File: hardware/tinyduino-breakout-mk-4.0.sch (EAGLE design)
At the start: 3 parts

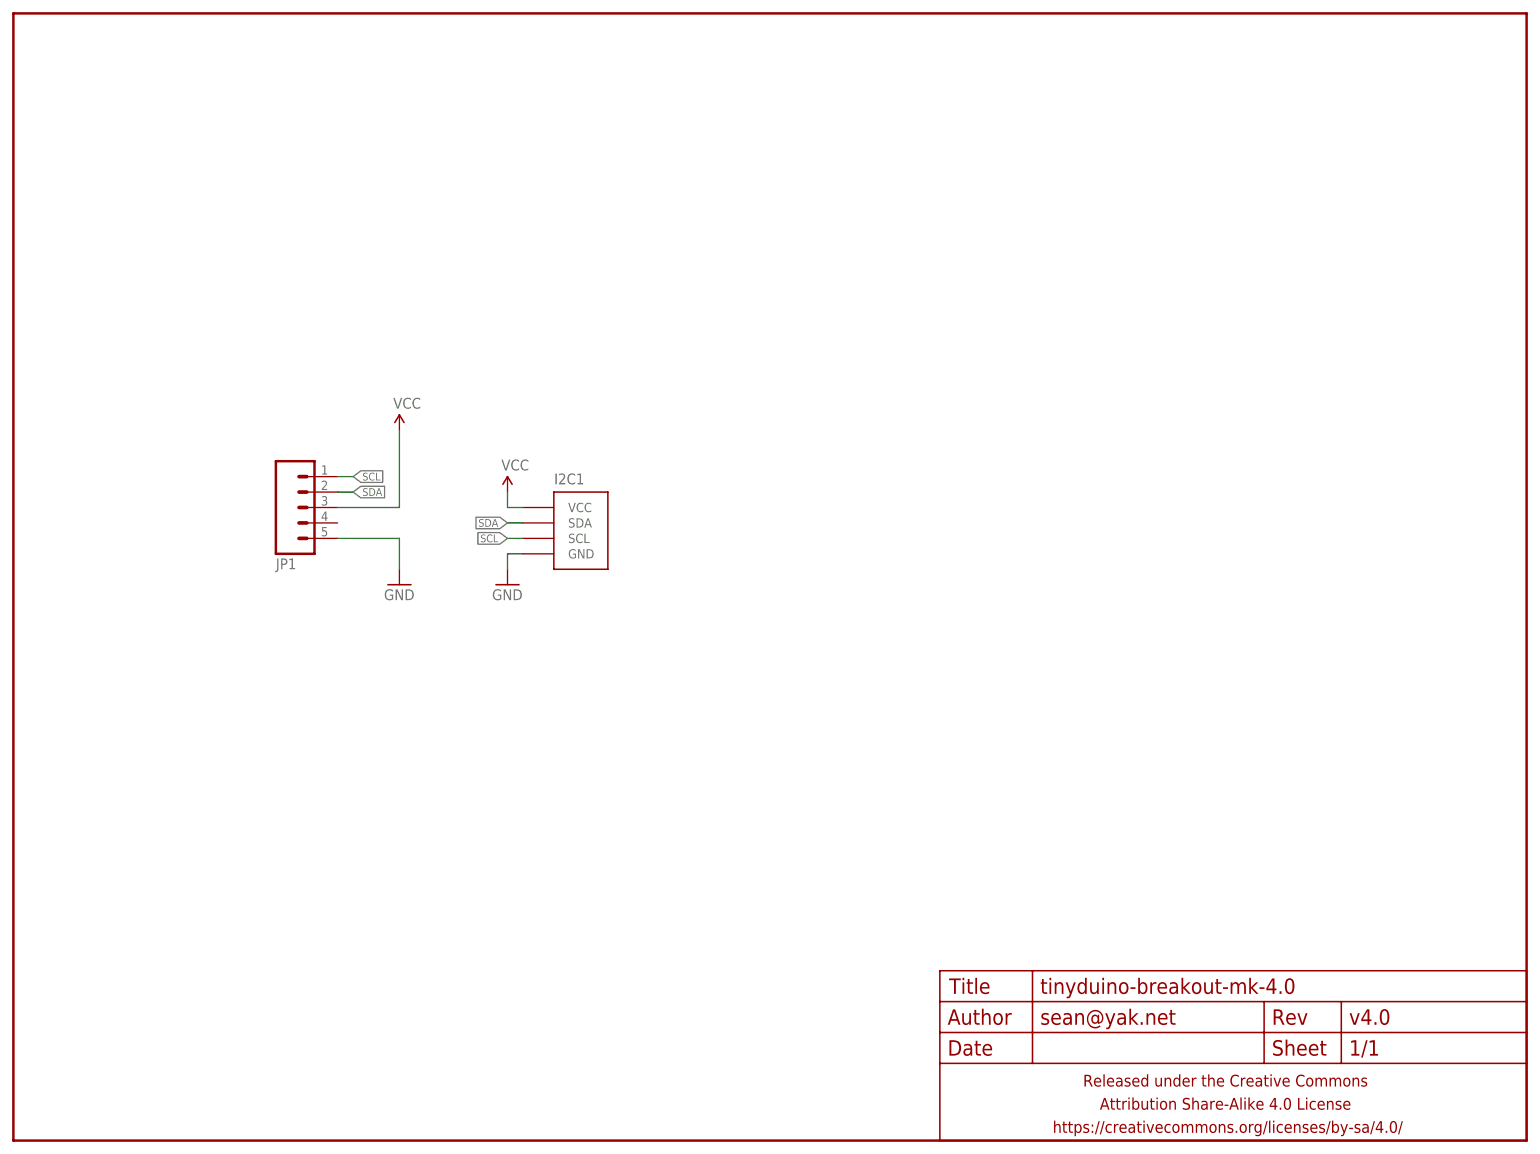
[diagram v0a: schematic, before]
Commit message: finished layout but unhappy w/choices
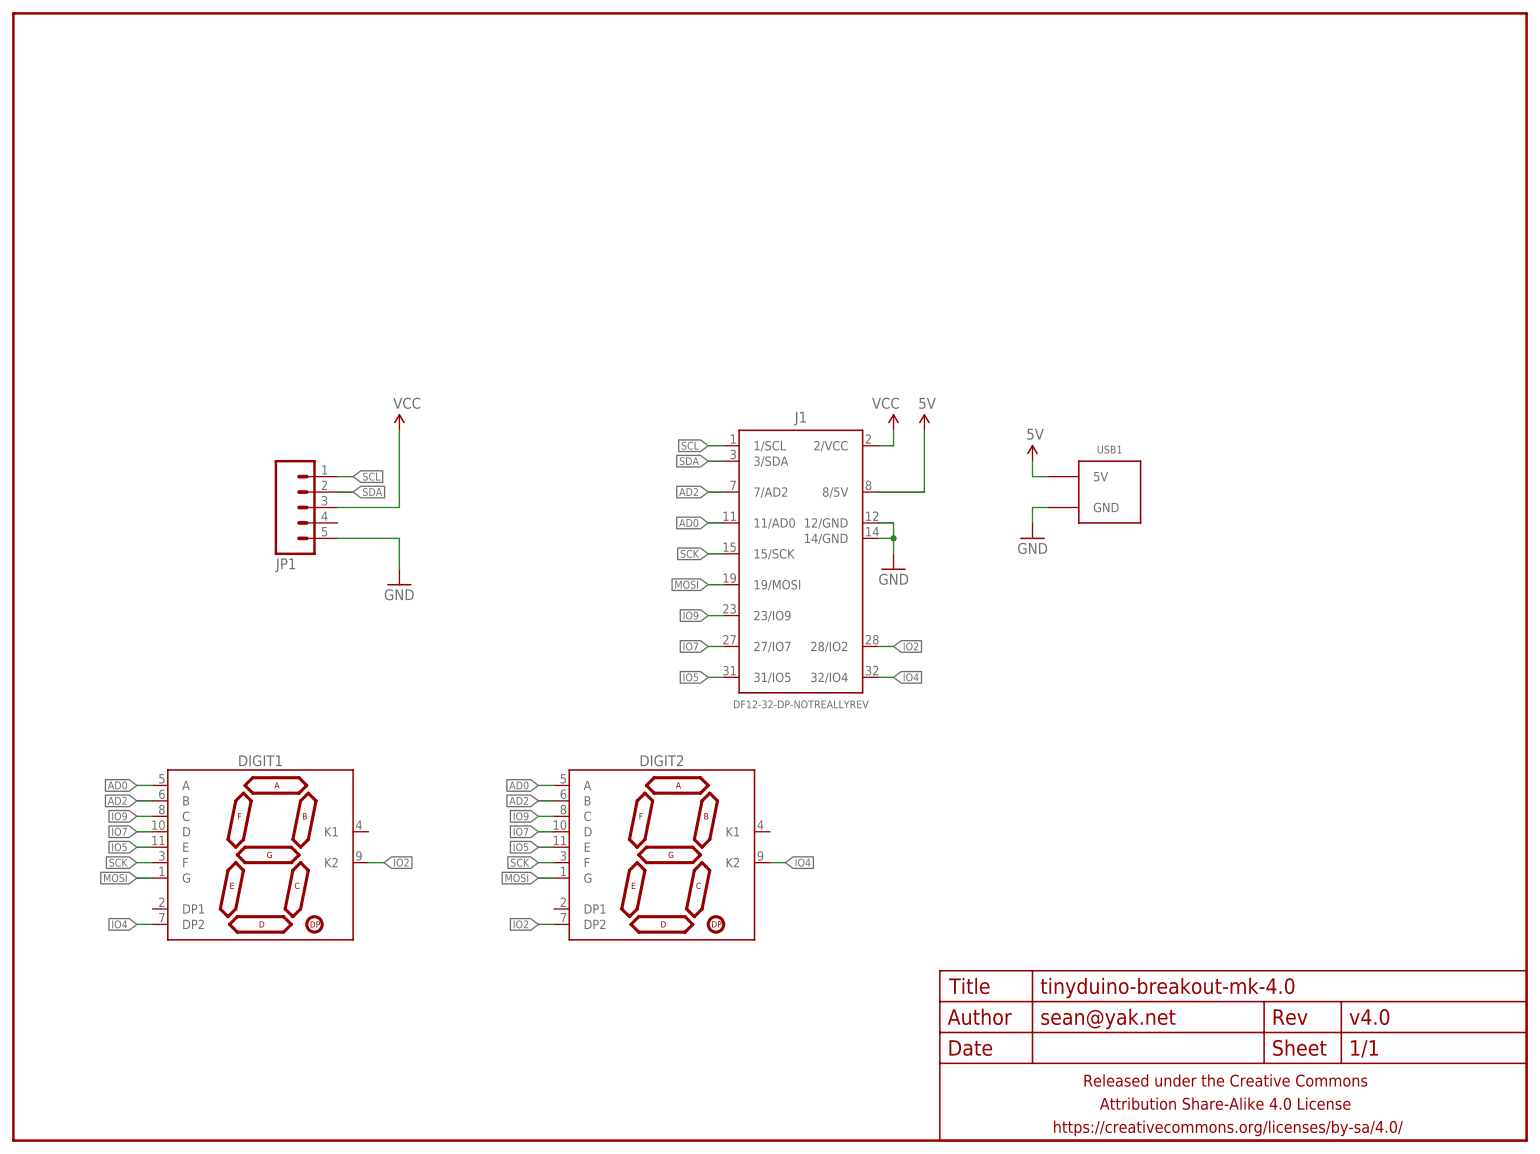
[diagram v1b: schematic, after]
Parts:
- removed I2C1: M04-I2CTINYDUINO-CONNECTOR-REV, A_butts:M04-I2CTINYDUINO-CONNECTOR-REV
- added DIGIT1, DIGIT2: 7SEG_1DIG_2DP7MM_CC_SMT, a_parts:7SEG_1DIG_2DP7MM_CC_SMT
- added J1: DF12-32-DP-NOTREALLYREV, a_parts:DF12-32-DP-NOTREALLYREV
- added USB1: USB_AB_PWRONLY, a_parts:USB_AB_PWRONLY
- JP1: value M05SMD-SHORT -> M05PTH-CENTERED; device A_butts:M05SMD-SHORT -> a_parts:M05PTH-CENTERED
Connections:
- new net 5V: J1.8/5V, USB1.5V
- new net AD0: DIGIT1.A, DIGIT2.A, J1.11/AD0
- new net AD2: DIGIT1.B, DIGIT2.B, J1.7/AD2
- new net IO2: DIGIT1.K2, DIGIT2.DP2, J1.28/IO2
- new net IO4: DIGIT1.DP2, DIGIT2.K2, J1.32/IO4
- new net IO5: DIGIT1.E, DIGIT2.E, J1.31/IO5
- new net IO7: DIGIT1.D, DIGIT2.D, J1.27/IO7
- new net IO9: DIGIT1.C, DIGIT2.C, J1.23/IO9
- new net MOSI: DIGIT1.G, DIGIT2.G, J1.19/MOSI
- new net SCK: DIGIT1.F, DIGIT2.F, J1.15/SCK
- net GND: now also J1.12/GND, J1.14/GND, USB1.GND; no longer I2C1.GND
- net SCL: now also J1.1/SCL; no longer I2C1.SCL
- net SDA: now also J1.3/SDA; no longer I2C1.SDA
- net VCC: now also J1.2/VCC; no longer I2C1.VCC
